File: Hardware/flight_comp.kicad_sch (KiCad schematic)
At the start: 1 part, among them U1 STM32F405RGTx

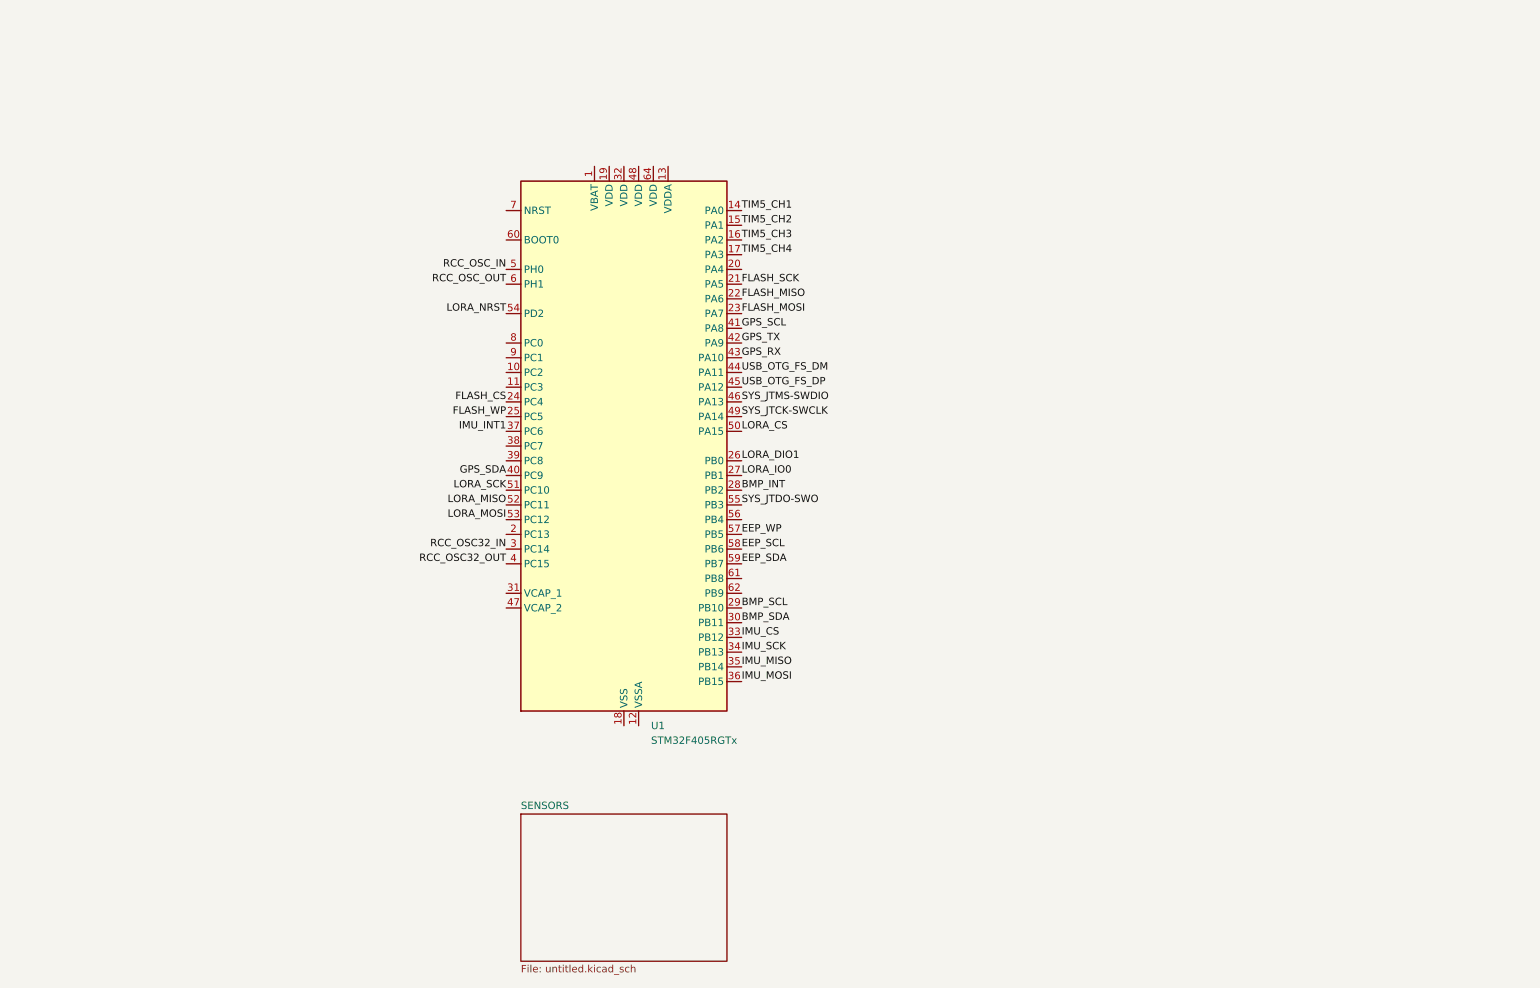
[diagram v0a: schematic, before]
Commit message: Power sch added
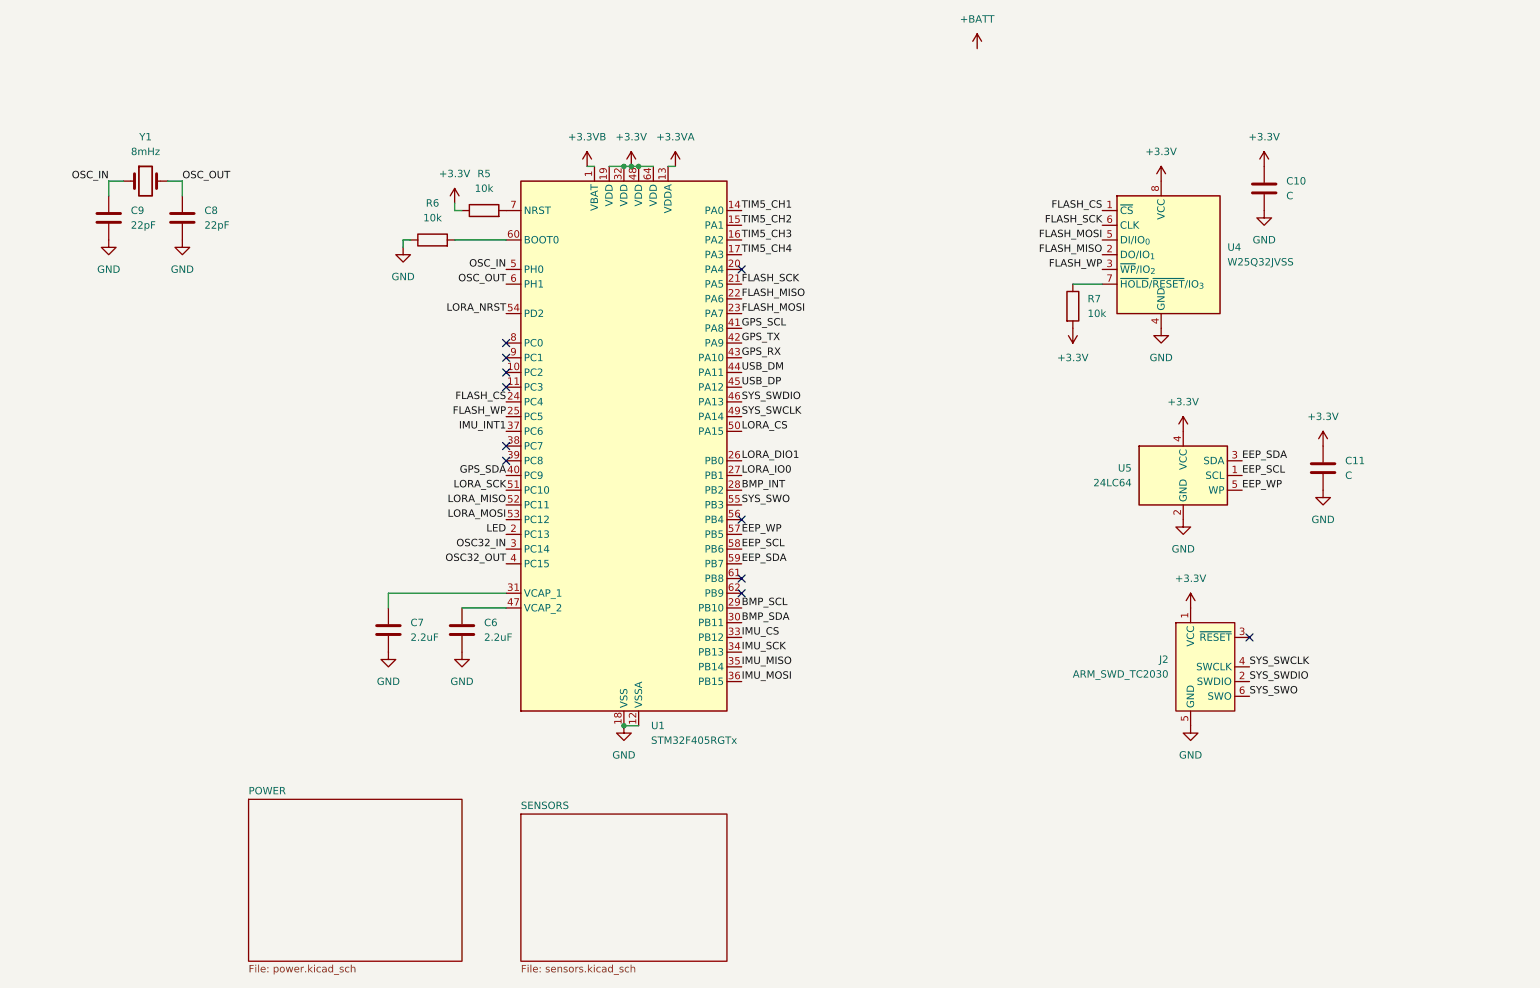
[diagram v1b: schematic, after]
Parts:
- added C10, C11: C, symbol Device:C
- added C6, C7: 2.2uF, symbol Device:C
- added C8, C9: 22pF, symbol Device:C
- added J2: ARM_SWD_TC2030, Connector:Tag-Connect_TC2030-IDC-NL_2x03_P1.27mm_Vertical, symbol Connector:Conn_ARM_SWD_TagConnect_TC2030-NL
- added R5, R6, R7: 10k, symbol Device:R
- added U4: W25Q32JVSS, Package_SO:SOIC-8_5.3x5.3mm_P1.27mm, symbol Memory_Flash:W25Q32JVSS
- added U5: 24LC64, Package_TO_SOT_SMD:SOT-23-5, symbol library:24LC64
- added Y1: 8mHz, Crystal:Crystal_SMD_5032-2Pin_5.0x3.2mm, symbol Device:Crystal
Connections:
- net EEP_SCL: now also U5.1 (SCL)
- net EEP_SDA: now also U5.3 (SDA)
- net EEP_WP: now also U5.5 (WP)
- net FLASH_CS: now also U4.1 (~{CS})
- net FLASH_MISO: now also U4.2 (DO/IO_{1})
- net FLASH_MOSI: now also U4.5 (DI/IO_{0})
- net FLASH_SCK: now also U4.6 (CLK)
- net FLASH_WP: now also U4.3 (~{WP}/IO_{2})
- net +3.3VB: now reaches U1.1 (VBAT)
- net GND: now reaches U1.12 (VSSA)
- net GND: now also U1.18 (VSS), U1.63 (VSS), C10.2, C11.2, C6.2, C7.2, C8.2, C9.2, J2.5 (GND), R6.1, U4.4 (GND), U5.2 (GND)
- net +3.3VA: now reaches U1.13 (VDDA)
- net +3.3V: now reaches U1.19 (VDD)
- net +3.3V: now also U1.32 (VDD), U1.48 (VDD), U1.64 (VDD), C10.1, C11.1, J2.1 (VCC), R5.1, R7.2, U4.8 (VCC), U5.4 (VCC)
- net LED: now reaches U1.2 (PC13)
- net at U1.31 (VCAP_1): now also C7.1
- net at U1.47 (VCAP_2): now also C6.1
- net at U1.60 (BOOT0): now also R6.2
- net at U1.7 (NRST): now also R5.2
- net RCC_OSC32_IN renamed OSC32_IN
- net RCC_OSC32_OUT renamed OSC32_OUT
- net RCC_OSC_IN renamed OSC_IN
- net OSC_IN: now also C9.1, Y1.1
- net RCC_OSC_OUT renamed OSC_OUT
- net OSC_OUT: now also C8.1, Y1.2
- net SYS_JTCK-SWCLK renamed SYS_SWCLK
- net SYS_SWCLK: now also J2.4 (SWCLK)
- net SYS_JTDO-SWO renamed SYS_SWO
- net SYS_SWO: now also J2.6 (SWO)
- net SYS_JTMS-SWDIO renamed SYS_SWDIO
- net SYS_SWDIO: now also J2.2 (SWDIO)
- net USB_OTG_FS_DM renamed USB_DM
- net USB_OTG_FS_DP renamed USB_DP
- new net: R7.1, U4.7 (~{HOLD}/~{RESET}/IO_{3})
- no-connect marks 0 -> 11
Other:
- added sheet POWER (power.kicad_sch)
- sheet SENSORS: file untitled.kicad_sch -> sensors.kicad_sch

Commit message: Changes in power system
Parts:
- added BT1: CR1220, Battery:BatteryHolder_Keystone_500, symbol Device:Battery_Cell
- added C20, C23: 22pF, symbol Device:C
- added C27, C28, C29, C30, C31, C32, C33: 0.1uF, symbol Device:C
- added J4: USB_C_Receptacle_USB2.0_16P, Connector_USB:USB_C_Receptacle_GCT_USB4110, symbol Connector:USB_C_Receptacle_USB2.0_16P
- added L2: L, symbol Device:L
- added R14: 4.7k, Resistor_SMD:R_0603_1608Metric, symbol Device:R
- added U8: USBLC6-2SC6, Package_TO_SOT_SMD:SOT-23-6, symbol Power_Protection:USBLC6-2SC6
- added Y2: 32.768 kHz, Crystal:Crystal_SMD_3215-2Pin_3.2x1.5mm, symbol Device:Crystal
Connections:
- net +3.3V: now also C28.1, C30.1, C31.1, C32.1, C33.1, L2.1
- net +3.3VA: now also C29.1, L2.2
- net +3.3VB: now also BT1.1 (+), C27.1
- net GND: now also BT1.2 (-), C20.2, C23.2, C27.2, C28.2, C29.2, C30.2, C31.2, C32.2, C33.2, J4.A1 (GND), J4.A12 (GND), J4.B1 (GND), J4.B12 (GND), J4.S1 (SHIELD), R14.2, U8.2 (GND)
- net OSC32_IN: now also C20.1, Y2.1
- net OSC32_OUT: now also C23.1, Y2.2
- net USB_DM: now also U8.6 (I/O1)
- net USB_DP: now also U8.4 (I/O2)
- new net: J4.A5 (CC1), J4.B5 (CC2), R14.1
- new net: J4.A6 (D+), J4.B6 (D+), U8.3 (I/O2)
- new net: J4.A7 (D-), J4.B7 (D-), U8.1 (I/O1)
- new net VBUS: J4.A4 (VBUS), J4.A9 (VBUS), J4.B4 (VBUS), J4.B9 (VBUS), U8.5 (VBUS)
- no-connect marks 11 -> 13
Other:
- moved on the sheet: C10, C11, J2, R7, U4, U5
